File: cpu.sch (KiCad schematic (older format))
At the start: 27 parts, among them J1 SWD_boctok, P5 ISO7421D, U6 STM32F410RBTx, U7 24C64, Y2 cx5032ga

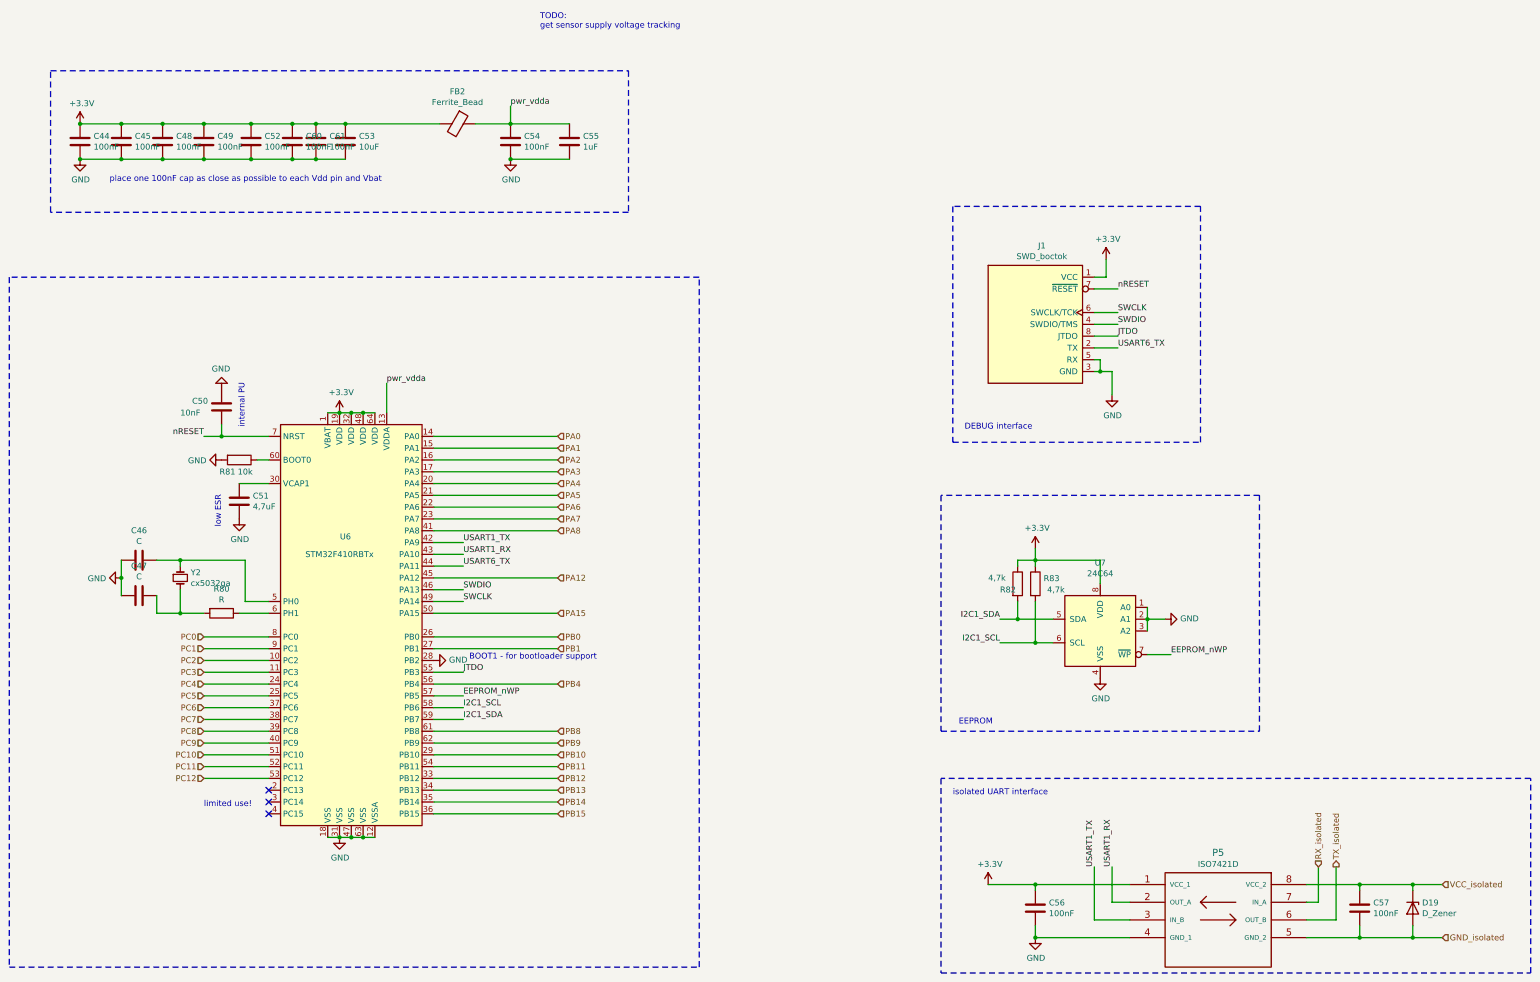
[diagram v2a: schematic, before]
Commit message: added missing component values working on BOM
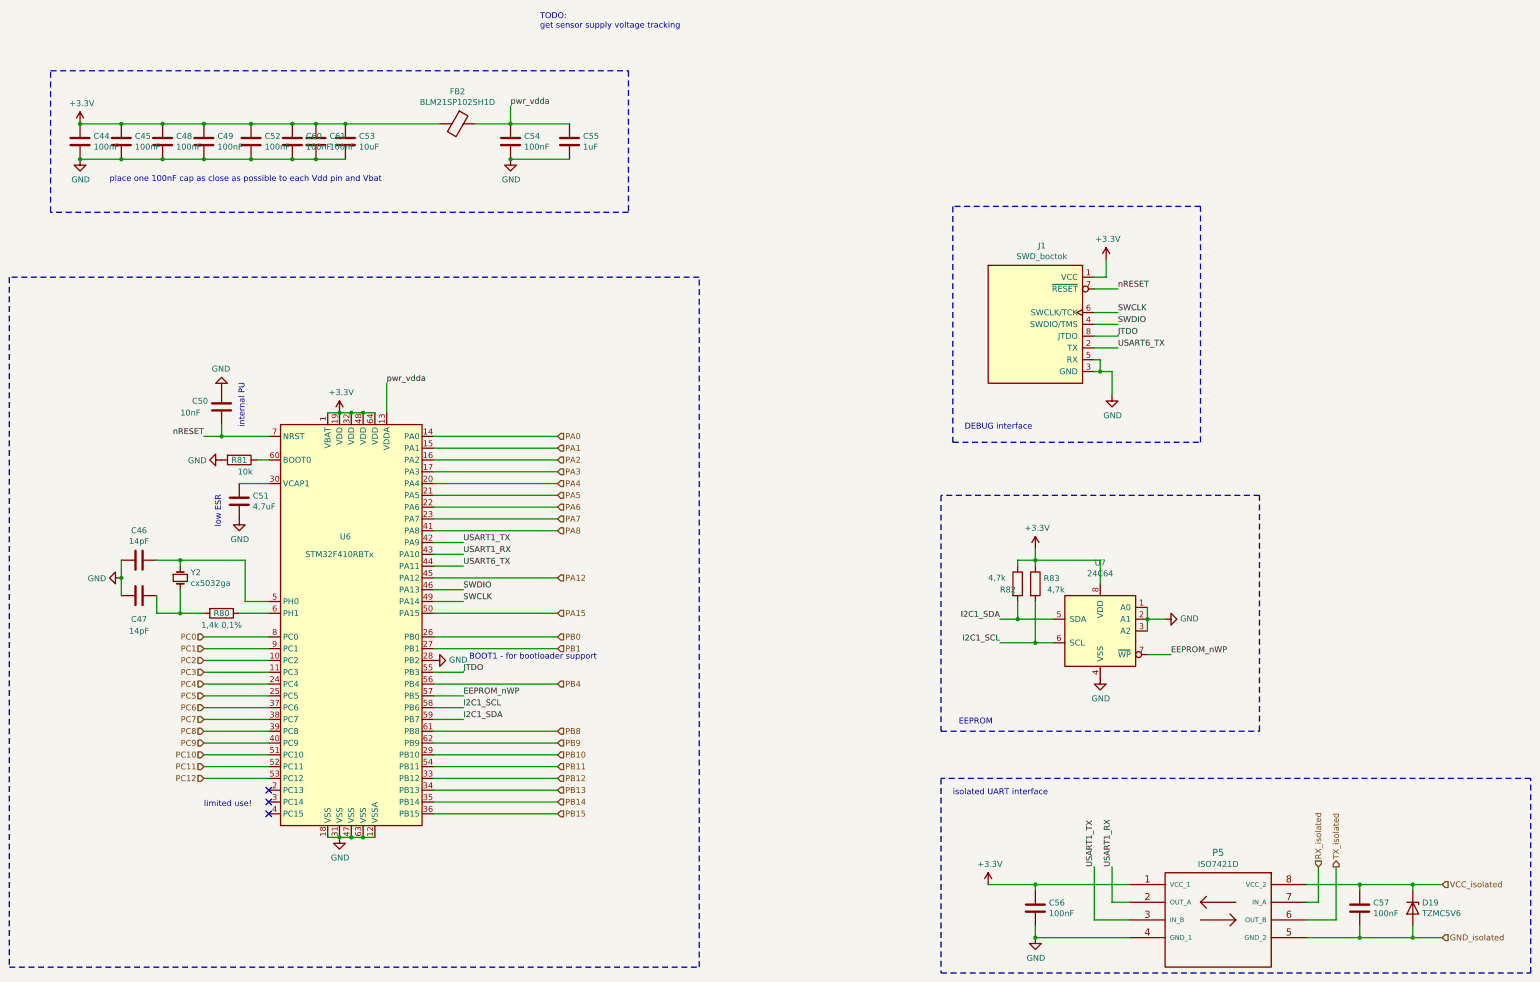
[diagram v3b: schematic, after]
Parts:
- C44, C45, C48, C49, C52, C54, C56, C57, C60, C61: Mouser (none) -> 80-C0805C104Z3V
- C46, C47: value C -> 14pF
- C51: Mouser (none) -> 755-TCSOPL1A226M8R
- C55: Mouser (none) -> 80-C0805C105M4R
- D19: value D_Zener -> TZMC5V6
- FB2: value Ferrite_Bead -> BLM21SP102SH1D
- R80: value R -> 1,4k 0,1%
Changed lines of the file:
@@
 F 2 "Capacitor_SMD:C_0805_2012Metric" H 2538 2300 50  0001 C CNN
 F 3 "~" H 2500 2450 50  0001 C CNN
+F 4 "80-C0805C104Z3V " H 2500 2450 50  0001 C CNN "Mouser"
 	1    2500 2450
 	1    0    0    -1
@@
 F 2 "Capacitor_SMD:C_0805_2012Metric" H 2888 2300 50  0001 C CNN
 F 3 "~" H 2850 2450 50  0001 C CNN
+F 4 "80-C0805C104Z3V " H 2850 2450 50  0001 C CNN "Mouser"
 	1    2850 2450
 	1    0    0    -1
@@
 F 2 "Capacitor_SMD:C_0805_2012Metric" H 3238 2300 50  0001 C CNN
 F 3 "~" H 3200 2450 50  0001 C CNN
+F 4 "80-C0805C104Z3V " H 3200 2450 50  0001 C CNN "Mouser"
 	1    3200 2450
 	1    0    0    -1
@@
 F 2 "Capacitor_SMD:C_0805_2012Metric" H 3588 2300 50  0001 C CNN
 F 3 "~" H 3550 2450 50  0001 C CNN
+F 4 "80-C0805C104Z3V " H 3550 2450 50  0001 C CNN "Mouser"
 	1    3550 2450
 	1    0    0    -1
@@
 F 2 "Capacitor_SMD:C_0805_2012Metric" H 3988 2300 50  0001 C CNN
 F 3 "~" H 3950 2450 50  0001 C CNN
+F 4 "80-C0805C104Z3V " H 3950 2450 50  0001 C CNN "Mouser"
 	1    3950 2450
 	1    0    0    -1
@@
 F 2 "Capacitor_SMD:C_0805_2012Metric" H 6688 2300 50  0001 C CNN
 F 3 "~" H 6650 2450 50  0001 C CNN
+F 4 "80-C0805C105M4R " H 6650 2450 50  0001 C CNN "Mouser"
 	1    6650 2450
 	1    0    0    -1
@@
 F 2 "Capacitor_SMD:C_0805_2012Metric" H 6188 2300 50  0001 C CNN
 F 3 "~" H 6150 2450 50  0001 C CNN
+F 4 "80-C0805C104Z3V " H 6150 2450 50  0001 C CNN "Mouser"
 	1    6150 2450
 	1    0    0    -1
@@
 P 5700 2300
 F 0 "FB2" V 5426 2300 50  0000 C CNN
-F 1 "Ferrite_Bead" V 5517 2300 50  0000 C CNN
+F 1 "BLM21SP102SH1D" V 5517 2300 50  0000 C CNN
 F 2 "Inductor_SMD:L_0805_2012Metric" V 5630 2300 50  0001 C CNN
 F 3 "~" H 5700 2300 50  0001 C CNN
@@
 F 2 "Capacitor_SMD:C_0805_2012Metric" H 3888 5350 50  0001 C CNN
 F 3 "~" H 3850 5500 50  0001 C CNN
+F 4 "755-TCSOPL1A226M8R " H 3850 5500 50  0001 C CNN "Mouser"
 	1    3850 5500
 	1    0    0    -1
@@
 P 3000 6000
 F 0 "C46" V 2748 6000 50  0000 C CNN
-F 1 "C" V 2839 6000 50  0000 C CNN
+F 1 "14pF" V 2839 6000 50  0000 C CNN
 F 2 "Capacitor_SMD:C_0805_2012Metric" H 3038 5850 50  0001 C CNN
 F 3 "~" H 3000 6000 50  0001 C CNN
@@
 U 1 1 5BD0CDAD
 P 3000 6300
-F 0 "C47" V 2748 6300 50  0000 C CNN
-F 1 "C" V 2839 6300 50  0000 C CNN
+F 0 "C47" V 3200 6300 50  0000 C CNN
+F 1 "14pF" V 3300 6300 50  0000 C CNN
 F 2 "Capacitor_SMD:C_0805_2012Metric" H 3038 6150 50  0001 C CNN
 F 3 "~" H 3000 6300 50  0001 C CNN
@@
 U 1 1 5BD0CE1E
 P 3700 6450
-F 0 "R80" V 3493 6450 50  0000 C CNN
-F 1 "R" V 3584 6450 50  0000 C CNN
+F 0 "R80" V 3700 6450 50  0000 C CNN
+F 1 "1,4k 0,1%" V 3800 6450 50  0000 C CNN
 F 2 "Resistor_SMD:R_0805_2012Metric" V 3630 6450 50  0001 C CNN
 F 3 "~" H 3700 6450 50  0001 C CNN
@@
 U 1 1 5BD28D3E
 P 3850 5150
-F 0 "R81" V 3950 5050 50  0000 C CNN
+F 0 "R81" V 3850 5150 50  0000 C CNN
 F 1 "10k" V 3950 5200 50  0000 C CNN
 F 2 "Resistor_SMD:R_0805_2012Metric" V 3780 5150 50  0001 C CNN
@@
 F 2 "Capacitor_SMD:C_0805_2012Metric" H 10638 8800 50  0001 C CNN
 F 3 "~" H 10600 8950 50  0001 C CNN
+F 4 "80-C0805C104Z3V " H 10600 8950 50  0001 C CNN "Mouser"
 	1    10600 8950
 	1    0    0    -1
@@
 F 2 "Capacitor_SMD:C_0805_2012Metric" H 13388 8800 50  0001 C CNN
 F 3 "~" H 13350 8950 50  0001 C CNN
+F 4 "80-C0805C104Z3V " H 13350 8950 50  0001 C CNN "Mouser"
 	1    13350 8950
 	1    0    0    -1
@@
 P 13800 8950
 F 0 "D19" V 13754 9029 50  0000 L CNN
-F 1 "D_Zener" V 13845 9029 50  0000 L CNN
+F 1 "TZMC5V6" V 13845 9029 50  0000 L CNN
 F 2 "Diode_SMD:D_MELF" H 13800 8950 50  0001 C CNN
 F 3 "~" H 13800 8950 50  0001 C CNN
@@
 F 2 "Capacitor_SMD:C_0805_2012Metric" H 4338 2300 50  0001 C CNN
 F 3 "~" H 4300 2450 50  0001 C CNN
+F 4 "80-C0805C104Z3V " H 4300 2450 50  0001 C CNN "Mouser"
 	1    4300 2450
 	1    0    0    -1
@@
 F 2 "Capacitor_SMD:C_0805_2012Metric" H 4538 2300 50  0001 C CNN
 F 3 "~" H 4500 2450 50  0001 C CNN
+F 4 "80-C0805C104Z3V " H 4500 2450 50  0001 C CNN "Mouser"
 	1    4500 2450
 	1    0    0    -1

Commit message: cleaned BOMs
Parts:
- C46, C47: Mouser (none) -> 80-C0805C130J5G
- C50: Mouser (none) -> 80-C0805C103K1R
- C53: Mouser (none) -> 80-C1206C106K4RAUTO
- D19: Mouser (none) -> 78-TZMC5.6
- FB2: Mouser (none) -> 81-BLM21SP102SH1D
- J1: Mouser (none) -> 855-M20-8760442
- P5: Mouser (none) -> 595-ISO7421DR
- R80: Mouser (none) -> 603-RT0805BRD071K4L
- R81: Mouser (none) -> 279-CRGCQ0805F10K
- R82, R83: Mouser (none) -> 71-CRCW08054K70FKEAC
- U6: Mouser (none) -> 511-STM32F410RBT6
- U7: Mouser (none) -> 511-M24C64-RMN6P
- Y2: Mouser (none) -> 581-CX5032GA08H0PST
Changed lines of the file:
@@
 F 2 "Capacitor_SMD:C_1206_3216Metric" H 4788 2300 50  0001 C CNN
 F 3 "~" H 4750 2450 50  0001 C CNN
+F 4 "80-C1206C106K4RAUTO " H 4750 2450 50  0001 C CNN "Mouser"
 	1    4750 2450
 	1    0    0    -1
@@
 F 2 "Inductor_SMD:L_0805_2012Metric" V 5630 2300 50  0001 C CNN
 F 3 "~" H 5700 2300 50  0001 C CNN
+F 4 "81-BLM21SP102SH1D" H 5700 2300 50  0001 C CNN "Mouser"
 	1    5700 2300
 	0    1    1    0
@@
 F 2 "Capacitor_SMD:C_0805_2012Metric" H 3738 4550 50  0001 C CNN
 F 3 "~" H 3700 4700 50  0001 C CNN
+F 4 "80-C0805C103K1R" H 3700 4700 50  0001 C CNN "Mouser"
 	1    3700 4700
 	1    0    0    -1
@@
 F 2 "Capacitor_SMD:C_0805_2012Metric" H 3038 5850 50  0001 C CNN
 F 3 "~" H 3000 6000 50  0001 C CNN
+F 4 "80-C0805C130J5G" H 3000 6000 50  0001 C CNN "Mouser"
 	1    3000 6000
 	0    1    1    0
@@
 F 2 "Capacitor_SMD:C_0805_2012Metric" H 3038 6150 50  0001 C CNN
 F 3 "~" H 3000 6300 50  0001 C CNN
+F 4 "80-C0805C130J5G" H 3000 6300 50  0001 C CNN "Mouser"
 	1    3000 6300
 	0    1    1    0
@@
 F 2 "Resistor_SMD:R_0805_2012Metric" V 3630 6450 50  0001 C CNN
 F 3 "~" H 3700 6450 50  0001 C CNN
+F 4 "603-RT0805BRD071K4L" H 3700 6450 50  0001 C CNN "Mouser"
 	1    3700 6450
 	0    1    1    0
@@
 F 2 "boctok_footprints:swd_boctok" H 10650 3450 50  0001 L TNN
 F 3 "http://infocenter.arm.com/help/topic/com.arm.doc.faqs/attached/13634/cortex_debug_connectors.pdf" V 10250 2750 50  0001 C CNN
+F 4 "855-M20-8760442" H 10600 4000 50  0001 C CNN "Mouser"
 	1    10600 4000
 	1    0    0    -1
@@
 F 2 "Resistor_SMD:R_0805_2012Metric" V 3780 5150 50  0001 C CNN
 F 3 "~" H 3850 5150 50  0001 C CNN
+F 4 "279-CRGCQ0805F10K" H 3850 5150 50  0001 C CNN "Mouser"
 	1    3850 5150
 	0    1    1    0
@@
 F 2 "Resistor_SMD:R_0805_2012Metric" V 10380 6200 50  0001 C CNN
 F 3 "~" H 10450 6200 50  0001 C CNN
+F 4 "71-CRCW08054K70FKEAC " H 10450 6200 50  0001 C CNN "Mouser"
 	1    10450 6200
 	1    0    0    -1
@@
 F 2 "Resistor_SMD:R_0805_2012Metric" V 10530 6200 50  0001 C CNN
 F 3 "~" H 10600 6200 50  0001 C CNN
+F 4 "71-CRCW08054K70FKEAC " H 10600 6200 50  0001 C CNN "Mouser"
 	1    10600 6200
 	1    0    0    -1
@@
 F 2 "boctok_footprints:ISO7421D" H 12150 8700 60  0001 C CNN
 F 3 "" H 12150 9050 60  0000 C CNN
+F 4 "595-ISO7421DR" H 12150 9050 50  0001 C CNN "Mouser"
 	1    12150 9050
 	1    0    0    -1
@@
 F 2 "Package_QFP:LQFP-64_10x10mm_P0.5mm" H 4200 4850 50  0001 R CNN
 F 3 "http://www.st.com/st-web-ui/static/active/en/resource/technical/document/datasheet/DM00214043.pdf" H 4800 6550 50  0001 C CNN
+F 4 "511-STM32F410RBT6" H 4800 6550 50  0001 C CNN "Mouser"
 	1    4800 6550
 	1    0    0    -1
@@
 F 2 "boctok_footprints:24C64" H 11750 6150 50  0001 C CNN
 F 3 "http://www.cypress.com/file/41651/download" H 10950 6950 50  0001 C CNN
+F 4 "511-M24C64-RMN6P" H 11150 6600 50  0001 C CNN "Mouser"
 	1    11150 6600
 	-1   0    0    -1
@@
 F 2 "Diode_SMD:D_MELF" H 13800 8950 50  0001 C CNN
 F 3 "~" H 13800 8950 50  0001 C CNN
+F 4 "78-TZMC5.6" H 13800 8950 50  0001 C CNN "Mouser"
 	1    13800 8950
 	0    1    1    0
@@
 F 2 "boctok_footprints:cx5032" H 3250 6350 50  0001 C CNN
 F 3 "~" H 3350 6150 50  0001 C CNN
+F 4 "581-CX5032GA08H0PST" H 3350 6150 50  0001 C CNN "Mouser"
 	1    3350 6150
 	0    1    1    0
